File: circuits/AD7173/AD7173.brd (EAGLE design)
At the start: 21.4 x 31.2 mm, 35 parts, among them IC1 AD7173, IC2 ADP1720, IC3 ADP1720ARMZ-5, IC4 ADR445BR, Q1 FA-20H

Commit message: upadted AD7173 breakout board
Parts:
- added C16: 4.7uF, rcl:C0402
- turned C15 to 0 degrees
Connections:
- net GND: now also C16.2
- net N$28: now also C16.1
- net N$30: now also C15.1
- net VIN: no longer C15.1
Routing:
- net N$28: track 16.0 -> 18.4 mm
- net VIN: track 34.1 -> 32.4 mm
- net N$30: track 7.29 -> 8.74 mm
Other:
- board text added: "C16"
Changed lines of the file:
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@@
 <text x="13" y="10.9" size="0.6096" layer="122" font="vector" ratio="10" rot="MR180">AVDD</text>
 <text x="12.4" y="3.9" size="0.4064" layer="122" font="vector" ratio="10" rot="MR270">SJ3</text>
+<text x="3.8" y="3.3" size="0.4064" layer="121" font="vector" ratio="10">C16</text>
 </plain>
 <attributes>
@@
 <element name="C14" library="rcl" package="C0402" value="4.7uF" x="15.3" y="3.3" rot="MR90"/>
 <element name="L1" library="inductors" package="0402" value="BLM15HB121SN1" x="7.9" y="7.9" rot="R180"/>
-<element name="C15" library="rcl" package="C0402" value="0.1uF" x="4.3" y="5.2" rot="R180"/>
+<element name="C15" library="rcl" package="C0402" value="0.1uF" x="4.3" y="5.2"/>
 <element name="SJ1" library="jumper" package="SJ" value="" x="14.2" y="8.4" rot="MR270"/>
 <element name="SJ2" library="jumper" package="SJ" value="" x="10.8" y="8.4" rot="MR270"/>
@@
 <element name="LED2" library="led" package="CHIP-LED0603" value="" x="10.8" y="6.7" rot="R270"/>
 <element name="R5" library="rcl" package="R0402" value="220" x="8.2" y="6.7" rot="R180"/>
+<element name="C16" library="rcl" package="C0402" value="4.7uF" x="4.3" y="2.7"/>
 </elements>
 <signals>
@@
 <wire x1="13.4" y1="18" x2="14.37" y2="18" width="0.254" layer="16"/>
 <wire x1="14.37" y1="18" x2="14.42" y2="18.05" width="0.254" layer="16"/>
+<contactref element="C16" pad="2"/>
 <wire x1="15.3" y1="3.95" x2="15.3" y2="3.45" width="0" layer="19" extent="1-16"/>
 </signal>
@@
 <contactref element="C13" pad="1"/>
 <contactref element="L1" pad="1"/>
-<contactref element="C15" pad="1"/>
 <wire x1="6.4" y1="5.55" x2="6.4" y2="3.45" width="0.254" layer="1"/>
-<wire x1="4.95" y1="5.2" x2="5.5" y2="5.2" width="0.254" layer="1"/>
-<wire x1="5.5" y1="5.2" x2="5.8" y2="5.5" width="0.254" layer="1"/>
-<wire x1="5.8" y1="5.5" x2="6.45" y2="5.5" width="0.254" layer="1"/>
-<wire x1="6.45" y1="5.5" x2="6.4" y2="5.55" width="0.254" layer="1"/>
 <wire x1="6.4" y1="5.55" x2="14.65" y2="5.55" width="0.254" layer="1"/>
 <wire x1="14.65" y1="5.55" x2="15.2" y2="6.1" width="0.254" layer="1"/>
@@
 <wire x1="7.4" y1="7.7" x2="7.4" y2="6.85" width="0.254" layer="1"/>
 <wire x1="7.4" y1="6.85" x2="7.55" y2="6.7" width="0.254" layer="1"/>
+<contactref element="C15" pad="1"/>
+<wire x1="3.65" y1="5.2" x2="3.65" y2="6.65" width="0.254" layer="1"/>
 </signal>
 <signal name="N$28">
@@
 <wire x1="10.8" y1="4.062" x2="10.8" y2="7.638" width="0.254" layer="16"/>
 <wire x1="10.8" y1="7.638" x2="14.2" y2="7.638" width="0.254" layer="16"/>
+<contactref element="C16" pad="1"/>
+<wire x1="3.65" y1="2.7" x2="3.2" y2="2.7" width="0.254" layer="1"/>
+<wire x1="3.2" y1="2.7" x2="1.79" y2="4.11" width="0.254" layer="1"/>
 </signal>
 <signal name="N$31">

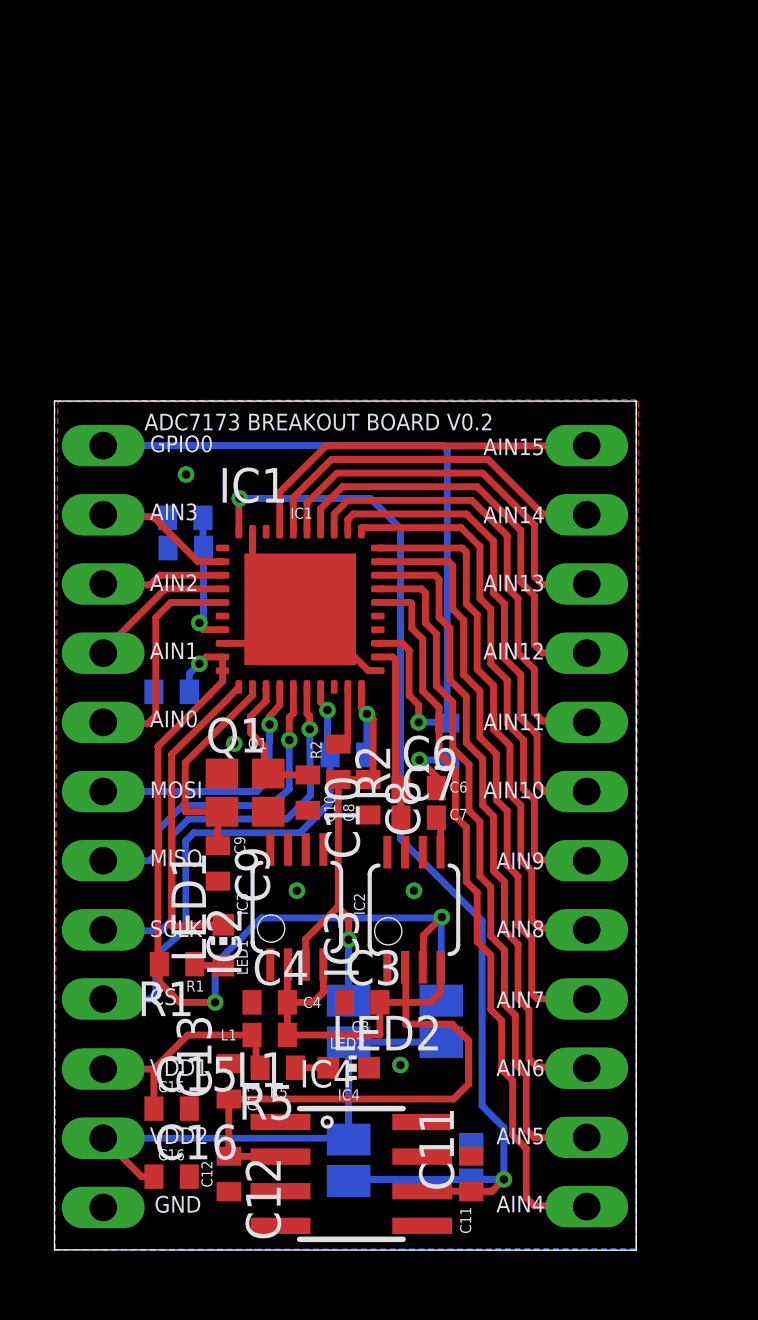
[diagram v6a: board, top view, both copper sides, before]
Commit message: updated AD7173 breakout board
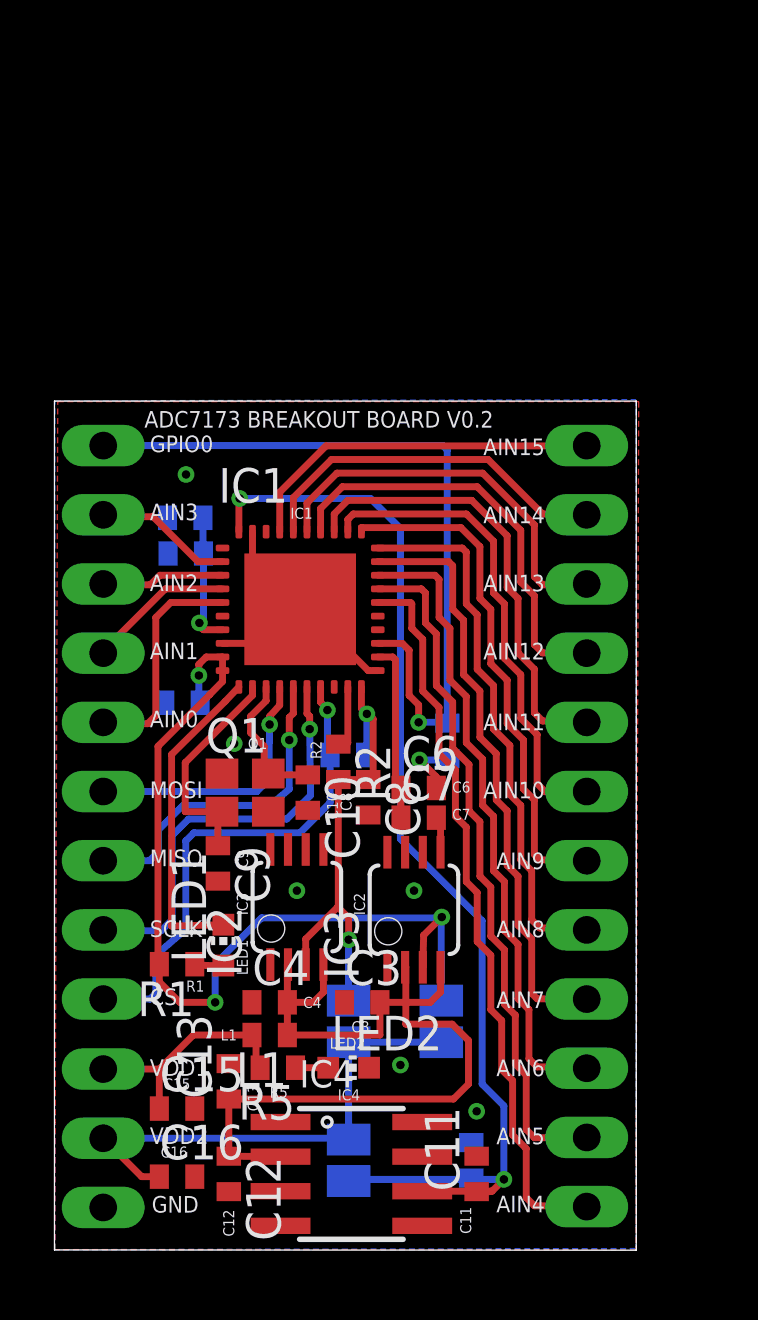
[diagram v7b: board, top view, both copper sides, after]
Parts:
- moved C1 0.57 mm to (4.70, 20.1)
- moved C5 0.20 mm to (4.82, 25.6)
- moved C15 0.20 mm to (4.50, 5.20)
- moved C16 0.20 mm to (4.50, 2.70)
- moved C11 0.20 mm to (15.5, 2.80)
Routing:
- net GND: vias 6 -> 7

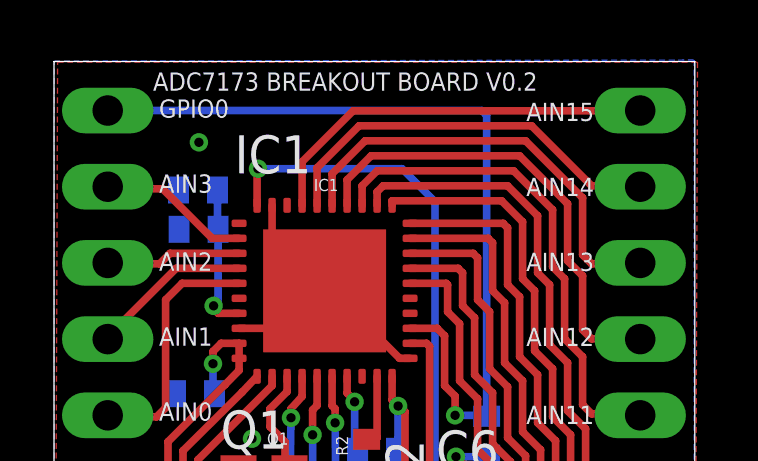
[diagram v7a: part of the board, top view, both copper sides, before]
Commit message: updated AD7173 breakout board
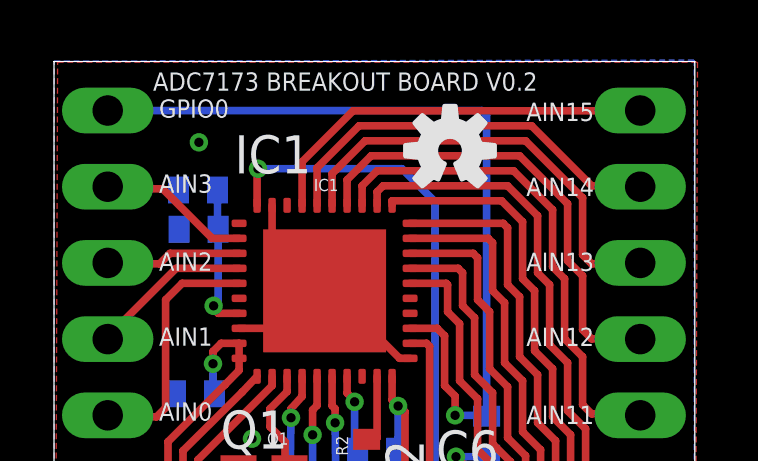
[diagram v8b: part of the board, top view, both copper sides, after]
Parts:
- added LOGO1: OSHW-LOGOS, SparkFun-Aesthetics:OSHW-LOGO-S
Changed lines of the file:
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@@
 <layer number="54" name="bGND_GNDA" color="7" fill="1" visible="no" active="yes"/>
 <layer number="56" name="wert" color="7" fill="1" visible="no" active="yes"/>
+<layer number="57" name="tCAD" color="7" fill="1" visible="no" active="no"/>
+<layer number="59" name="tCarbon" color="7" fill="1" visible="no" active="no"/>
+<layer number="60" name="bCarbon" color="7" fill="1" visible="no" active="no"/>
+<layer number="90" name="Modules" color="5" fill="1" visible="yes" active="yes"/>
 <layer number="91" name="Nets" color="2" fill="1" visible="no" active="no"/>
 <layer number="92" name="Busses" color="1" fill="1" visible="no" active="no"/>
@@
 <layer number="97" name="Info" color="7" fill="1" visible="no" active="no"/>
 <layer number="98" name="Guide" color="6" fill="1" visible="no" active="no"/>
+<layer number="99" name="SpiceOrder" color="7" fill="1" visible="no" active="no"/>
 <layer number="100" name="Muster" color="7" fill="1" visible="no" active="yes"/>
 <layer number="101" name="Patch_Top" color="7" fill="1" visible="no" active="yes"/>
@@
 <layer number="110" name="fp0" color="7" fill="1" visible="no" active="yes"/>
 <layer number="111" name="border" color="7" fill="1" visible="no" active="yes"/>
+<layer number="112" name="tSilk" color="7" fill="1" visible="yes" active="yes"/>
+<layer number="113" name="IDFDebug" color="4" fill="1" visible="yes" active="yes"/>
 <layer number="116" name="Patch_BOT" color="7" fill="1" visible="no" active="yes"/>
 <layer number="121" name="_tsilk" color="14" fill="1" visible="yes" active="yes"/>
@@
 <layer number="125" name="_tNames" color="14" fill="1" visible="no" active="yes"/>
 <layer number="126" name="_bNames" color="5" fill="1" visible="no" active="yes"/>
+<layer number="127" name="_tValues" color="7" fill="1" visible="yes" active="yes"/>
+<layer number="128" name="_bValues" color="7" fill="1" visible="yes" active="yes"/>
+<layer number="129" name="Mask" color="7" fill="1" visible="yes" active="yes"/>
 <layer number="131" name="tAdjust" color="7" fill="1" visible="no" active="yes"/>
 <layer number="132" name="bAdjust" color="7" fill="1" visible="no" active="yes"/>
 <layer number="144" name="DrillLegend" color="7" fill="1" visible="no" active="yes"/>
+<layer number="150" name="Notes" color="7" fill="1" visible="yes" active="yes"/>
 <layer number="151" name="HeatSink" color="7" fill="1" visible="no" active="yes"/>
+<layer number="152" name="_bDocu" color="7" fill="1" visible="yes" active="yes"/>
+<layer number="153" name="FabDoc1" color="7" fill="1" visible="yes" active="yes"/>
+<layer number="154" name="FabDoc2" color="7" fill="1" visible="yes" active="yes"/>
+<layer number="155" name="FabDoc3" color="7" fill="1" visible="yes" active="yes"/>
 <layer number="199" name="Contour" color="7" fill="1" visible="no" active="yes"/>
 <layer number="200" name="200bmp" color="7" fill="1" visible="no" active="yes"/>
@@
 <layer number="215" name="215bmp" color="7" fill="1" visible="no" active="yes"/>
 <layer number="216" name="216bmp" color="7" fill="1" visible="no" active="yes"/>
+<layer number="217" name="217bmp" color="18" fill="1" visible="no" active="no"/>
+<layer number="218" name="218bmp" color="19" fill="1" visible="no" active="no"/>
+<layer number="219" name="219bmp" color="20" fill="1" visible="no" active="no"/>
+<layer number="220" name="220bmp" color="21" fill="1" visible="no" active="no"/>
+<layer number="221" name="221bmp" color="22" fill="1" visible="no" active="no"/>
+<layer number="222" name="222bmp" color="23" fill="1" visible="no" active="no"/>
+<layer number="223" name="223bmp" color="24" fill="1" visible="no" active="no"/>
+<layer number="224" name="224bmp" color="25" fill="1" visible="no" active="no"/>
+<layer number="225" name="225bmp" color="7" fill="1" visible="yes" active="yes"/>
+<layer number="226" name="226bmp" color="7" fill="1" visible="yes" active="yes"/>
+<layer number="227" name="227bmp" color="7" fill="1" visible="yes" active="yes"/>
+<layer number="228" name="228bmp" color="7" fill="1" visible="yes" active="yes"/>
+<layer number="229" name="229bmp" color="7" fill="1" visible="yes" active="yes"/>
+<layer number="230" name="230bmp" color="7" fill="1" visible="yes" active="yes"/>
+<layer number="231" name="231bmp" color="7" fill="1" visible="yes" active="yes"/>
+<layer number="248" name="Housing" color="7" fill="1" visible="yes" active="yes"/>
+<layer number="249" name="Edge" color="7" fill="1" visible="yes" active="yes"/>
 <layer number="250" name="Descript" color="7" fill="1" visible="no" active="yes"/>
 <layer number="251" name="SMDround" color="7" fill="1" visible="no" active="yes"/>
 <layer number="254" name="cooling" color="7" fill="1" visible="no" active="yes"/>
+<layer number="255" name="routoute" color="7" fill="1" visible="yes" active="yes"/>
 </layers>
 <board>
@@
 <element name="R5" library="rcl" package="R0402" value="220" x="8.2" y="6.7" rot="R180"/>
 <element name="C16" library="rcl" package="C0402" value="4.7uF" x="4.5" y="2.7"/>
+<element name="LOGO1" library="SparkFun-Aesthetics" package="OSHW-LOGO-S" value="OSHW-LOGOS" x="13.2" y="28.2"/>
 </elements>
 <signals>
